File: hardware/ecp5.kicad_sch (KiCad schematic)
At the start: 6 parts, among them U3 ECP5U_12_CABGA256

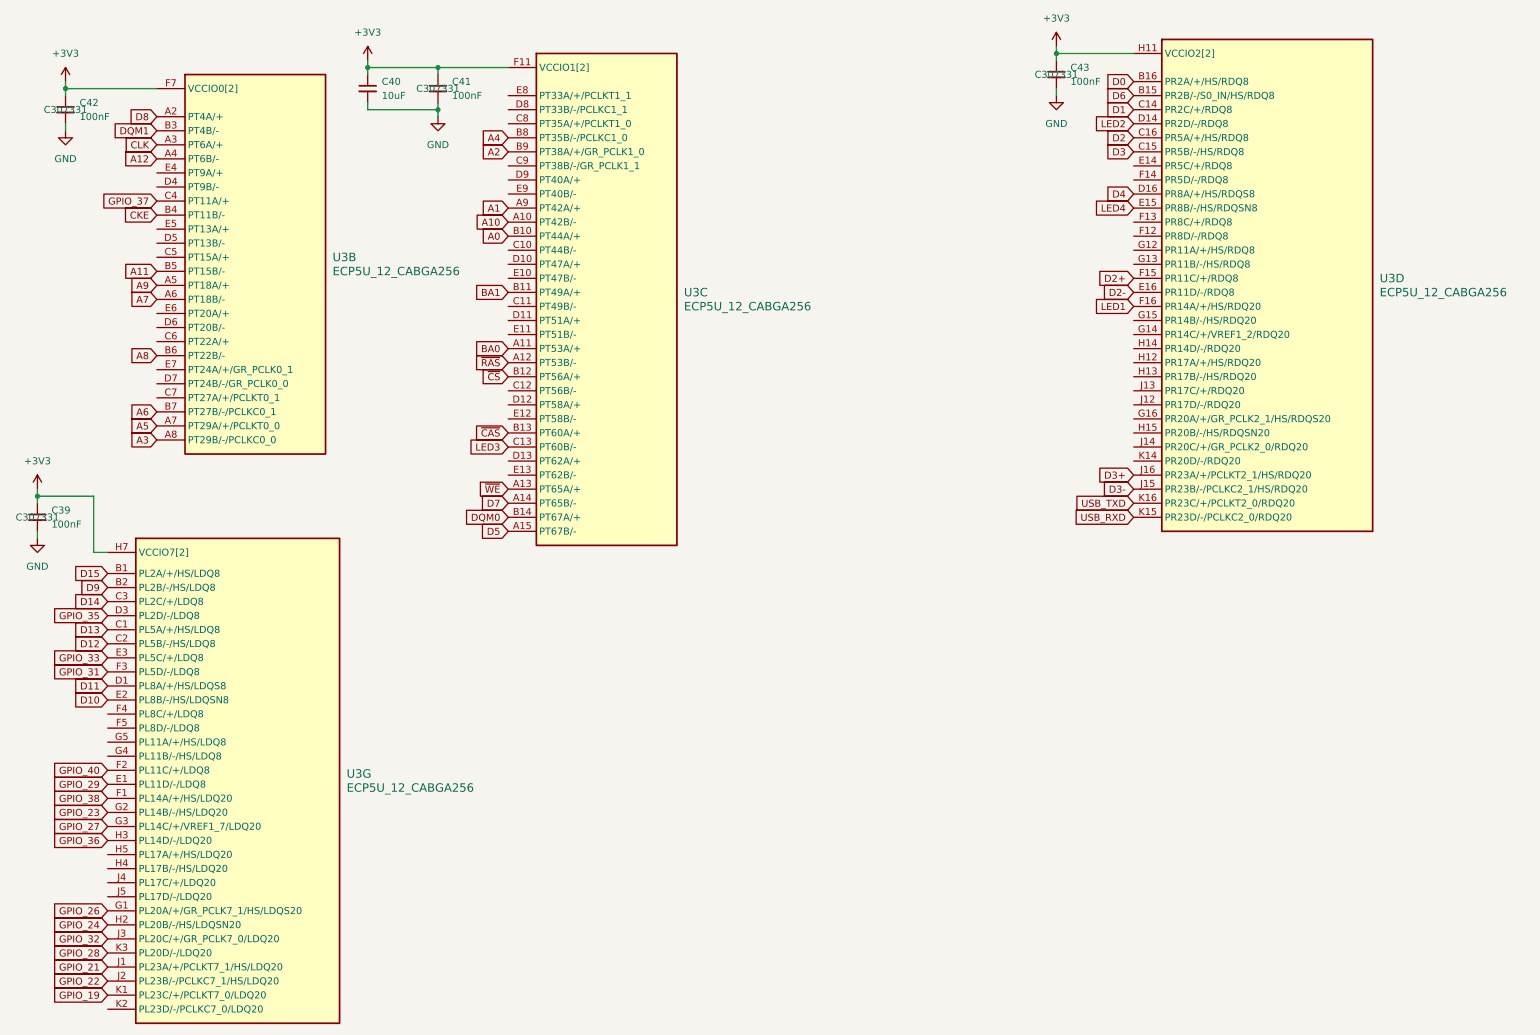
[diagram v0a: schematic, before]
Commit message: Fix level shifter EN voltage error
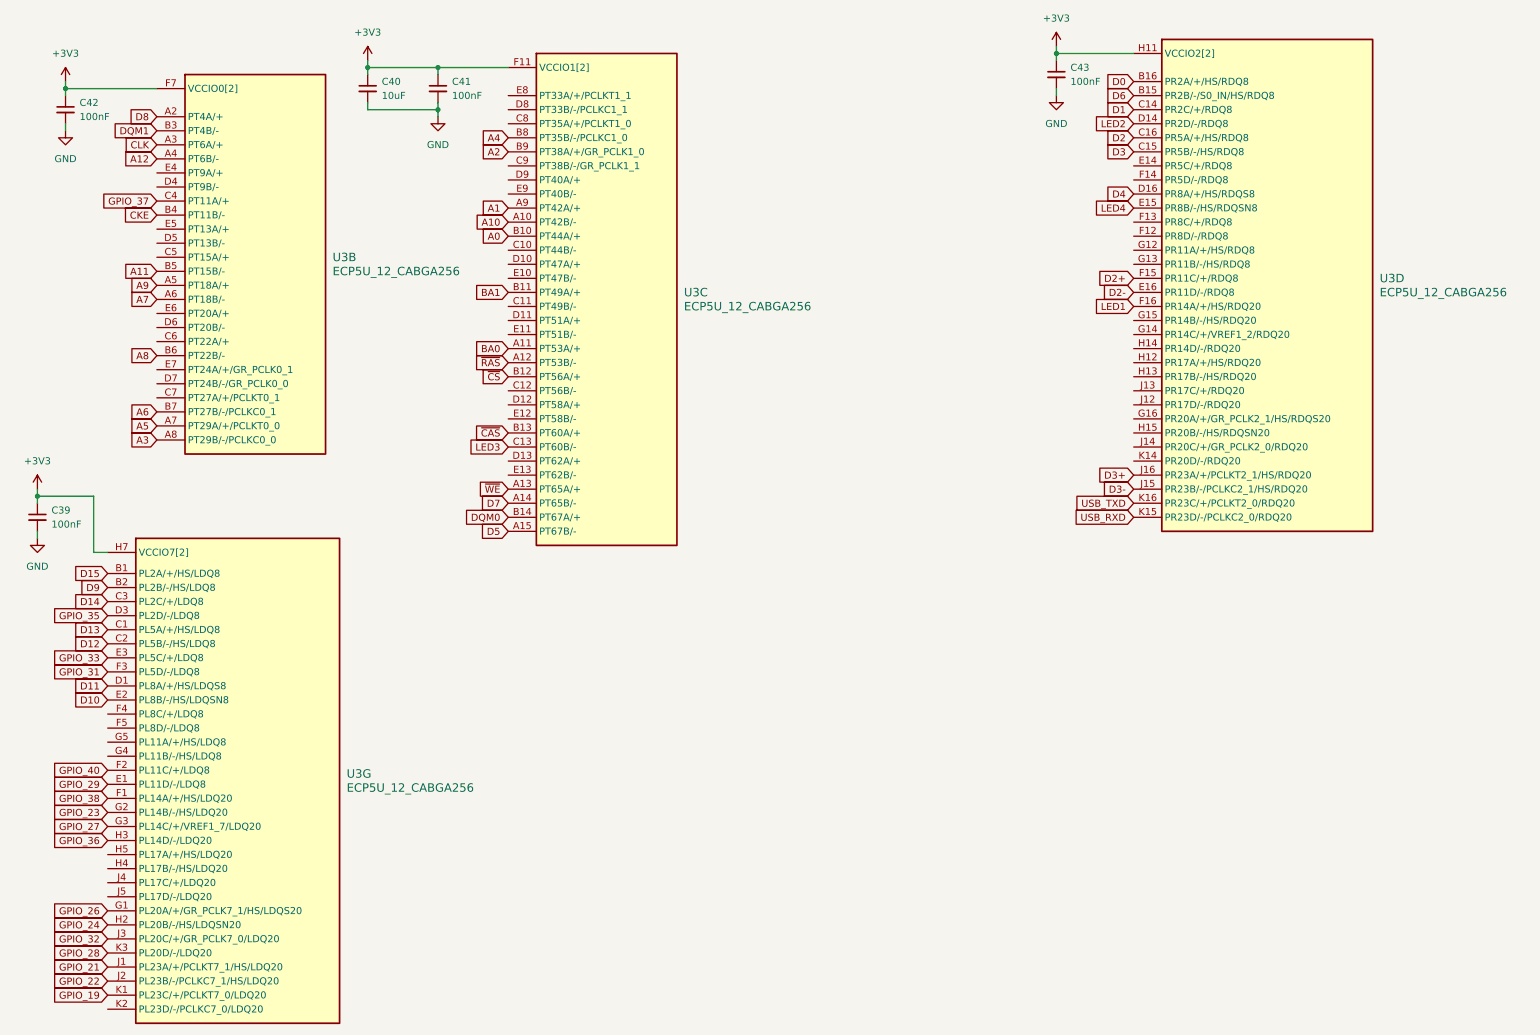
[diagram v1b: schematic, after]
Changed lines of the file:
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@@
 					(size 1.27 1.27)
 				)
+				(hide yes)
 			)
 		)
@@
 					(size 1.27 1.27)
 				)
+				(hide yes)
 			)
 		)
@@
 					(size 1.27 1.27)
 				)
+				(hide yes)
 			)
 		)
@@
 					(size 1.27 1.27)
 				)
-			)
-		)
+				(hide yes)
+			)
+		)

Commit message: Pre-prod fixes
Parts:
- added TP10, TP9: TestPoint, TestPoint:TestPoint_Pad_D2.0mm, symbol Connector:TestPoint
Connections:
- net GPIO_35: now also U3.E4 (PT9A/+); no longer U3.D3 (PL2D/-/LDQ8)
- net GPIO_37: now also U3.D4 (PT9B/-); no longer U3.C4 (PT11A/+)
- net LED2: now also U3.E15 (PR8B/-/HS/RDQSN8); no longer U3.D14 (PR2D/-/RDQ8)
- net LED3: now also U3.D14 (PR2D/-/RDQ8); no longer U3.C13 (PT60B/-)
- net LED4: now also U3.C13 (PT60B/-); no longer U3.E15 (PR8B/-/HS/RDQSN8)
- net at U3.C7 (PT27A/+/PCLKT0_1): now also TP9.1
- net at U3.C8 (PT35A/+/PCLKT1_0): now also TP10.1
- net LED5: now reaches U3.D13 (PT62A/+)
- net GPIO_19: no longer names the net of U3.K1 (PL23C/+/PCLKT7_0/LDQ20)
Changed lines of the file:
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@@
 	(wire
 		(pts
+			(xy 100.33 31.75) (xy 101.6 31.75)
+		)
+		(stroke
+			(width 0)
+			(type default)
+		)
+	)
+	(wire
+		(pts
 			(xy 21.59 31.75) (xy 21.59 33.02)
 		)
@@
 	(wire
 		(pts
+			(xy 34.29 81.28) (xy 38.1 81.28)
+		)
+		(stroke
+			(width 0)
+			(type default)
+		)
+	)
+	(wire
+		(pts
 			(xy 16.51 99.06) (xy 16.51 100.33)
 		)
@@
 		)
 	)
+	(global_label "GPIO_37"
+		(shape input)
+		(at 38.1 43.18 180)
+		(fields_autoplaced yes)
+		(effects
+			(font
+				(size 1.27 1.27)
+			)
+			(justify right)
+		)
+		(property "Intersheetrefs" "${INTERSHEET_REFS}"
+			(at 27.2529 43.18 0)
+			(effects
+				(font
+					(size 1.27 1.27)
+				)
+				(justify right)
+				(hide yes)
+			)
+		)
+	)
 	(global_label "GPIO_23"
 		(shape input)
@@
 		)
 	)
-	(global_label "GPIO_35"
-		(shape input)
-		(at 29.21 120.65 180)
-		(fields_autoplaced yes)
-		(effects
-			(font
-				(size 1.27 1.27)
-			)
-			(justify right)
-		)
-		(property "Intersheetrefs" "${INTERSHEET_REFS}"
-			(at 18.3629 120.65 0)
-			(effects
-				(font
-					(size 1.27 1.27)
-				)
-				(justify right)
-				(hide yes)
-			)
-		)
-	)
 	(global_label "D8"
 		(shape input)
@@
 		)
 	)
-	(global_label "GPIO_24"
+	(global_label "GPIO_35"
 		(shape input)
-		(at 29.21 176.53 180)
+		(at 38.1 40.64 180)
 		(fields_autoplaced yes)
 		(effects
@@
 		)
 		(property "Intersheetrefs" "${INTERSHEET_REFS}"
-			(at 18.3629 176.53 0)
+			(at 27.2529 40.64 0)
 			(effects
 				(font
@@
 		)
 	)
-	(global_label "D3"
+	(global_label "GPIO_24"
 		(shape input)
-		(at 214.63 36.83 180)
+		(at 29.21 176.53 180)
 		(fields_autoplaced yes)
 		(effects
@@
 		)
 		(property "Intersheetrefs" "${INTERSHEET_REFS}"
-			(at 209.1653 36.83 0)
+			(at 18.3629 176.53 0)
 			(effects
 				(font
@@
 		)
 	)
-	(global_label "GPIO_37"
+	(global_label "D3"
 		(shape input)
-		(at 38.1 45.72 180)
+		(at 214.63 36.83 180)
 		(fields_autoplaced yes)
 		(effects
@@
 		)
 		(property "Intersheetrefs" "${INTERSHEET_REFS}"
-			(at 27.2529 45.72 0)
+			(at 209.1653 36.83 0)
 			(effects
 				(font
@@
 		)
 	)
-	(global_label "LED2"
+	(global_label "LED3"
 		(shape input)
 		(at 214.63 31.75 180)
@@
 		)
 	)
-	(global_label "LED4"
+	(global_label "LED2"
 		(shape input)
 		(at 214.63 46.99 180)
@@
 		)
 	)
-	(global_label "GPIO_19"
+	(global_label "A0"
 		(shape input)
-		(at 29.21 189.23 180)
+		(at 101.6 52.07 180)
 		(fields_autoplaced yes)
 		(effects
@@
 		)
 		(property "Intersheetrefs" "${INTERSHEET_REFS}"
-			(at 18.3629 189.23 0)
+			(at 96.3167 52.07 0)
 			(effects
 				(font
@@
 		)
 	)
-	(global_label "A0"
+	(global_label "~{CS}"
 		(shape input)
-		(at 101.6 52.07 180)
+		(at 101.6 77.47 180)
 		(fields_autoplaced yes)
 		(effects
@@
 		)
 		(property "Intersheetrefs" "${INTERSHEET_REFS}"
-			(at 96.3167 52.07 0)
+			(at 96.1353 77.47 0)
 			(effects
 				(font
@@
 		)
 	)
-	(global_label "~{CS}"
+	(global_label "LED5"
 		(shape input)
-		(at 101.6 77.47 180)
+		(at 101.6 92.71 180)
 		(fields_autoplaced yes)
 		(effects
@@
 		)
 		(property "Intersheetrefs" "${INTERSHEET_REFS}"
-			(at 96.1353 77.47 0)
+			(at 93.9582 92.71 0)
 			(effects
 				(font
@@
 		)
 	)
-	(global_label "LED3"
+	(global_label "LED4"
 		(shape input)
 		(at 101.6 90.17 180)
@@
 	)
 	(symbol
+		(lib_id "Connector:TestPoint")
+		(at 34.29 81.28 90)
+		(unit 1)
+		(exclude_from_sim no)
+		(in_bom yes)
+		(on_board yes)
+		(dnp yes)
+		(property "Reference" "TP9"
+			(at 28.702 78.232 0)
+			(effects
+				(font
+					(size 1.27 1.27)
+				)
+				(justify right)
+			)
+		)
+		(property "Value" "TestPoint"
+			(at 26.162 78.232 0)
+			(effects
+				(font
+					(size 1.27 1.27)
+				)
+				(justify right)
+			)
+		)
+		(property "Footprint" "TestPoint:TestPoint_Pad_D2.0mm"
+			(at 34.29 76.2 0)
+			(effects
+				(font
+					(size 1.27 1.27)
+				)
+				(hide yes)
+			)
+		)
+		(property "Datasheet" "~"
+			(at 34.29 76.2 0)
+			(effects
+				(font
+					(size 1.27 1.27)
+				)
+				(hide yes)
+			)
+		)
+		(property "Description" "test point"
+			(at 34.29 81.28 0)
+			(effects
+				(font
+					(size 1.27 1.27)
+				)
+				(hide yes)
+			)
+		)
+		(pin "1"
+		)
+		(instances
+			(project "icepi-zero"
+				(path "/f88da08e-cf42-4d03-a08f-3f602fe6658d/17c9c9b3-f379-4e1f-a876-d3fcf0529a4d"
+					(reference "TP9")
+					(unit 1)
+				)
+			)
+		)
+	)
+	(symbol
 		(lib_id "josh:ECP5U_12_CABGA256")
 		(at 236.22 57.15 0)
@@
 					(unit 1)
 				)
+			)
+		)
+	)
+	(symbol
+		(lib_id "Connector:TestPoint")
+		(at 100.33 31.75 90)
+		(unit 1)
+		(exclude_from_sim no)
+		(in_bom yes)
+		(on_board yes)
+		(dnp yes)
+		(property "Reference" "TP10"
+			(at 94.742 28.702 0)
+			(effects
+				(font
+					(size 1.27 1.27)
+				)
+				(justify right)
+			)
+		)
+		(property "Value" "TestPoint"
+			(at 92.202 28.702 0)
+			(effects
+				(font
+					(size 1.27 1.27)
+				)
+				(justify right)
+			)
+		)
+		(property "Footprint" "TestPoint:TestPoint_Pad_D2.0mm"
+			(at 100.33 26.67 0)
+			(effects
+				(font
+					(size 1.27 1.27)
+				)
+				(hide yes)
+			)
+		)
+		(property "Datasheet" "~"
+			(at 100.33 26.67 0)
+			(effects
+				(font
+					(size 1.27 1.27)
+				)
+				(hide yes)
+			)
+		)
+		(property "Description" "test point"
+			(at 100.33 31.75 0)
+			(effects
+				(font
+					(size 1.27 1.27)
+				)
+				(hide yes)
+			)
+		)
+		(pin "1"
+		)
+		(instances
+			(project "icepi-zero"
+				(path "/f88da08e-cf42-4d03-a08f-3f602fe6658d/17c9c9b3-f379-4e1f-a876-d3fcf0529a4d"
+					(reference "TP10")
+					(unit 1)
+				)

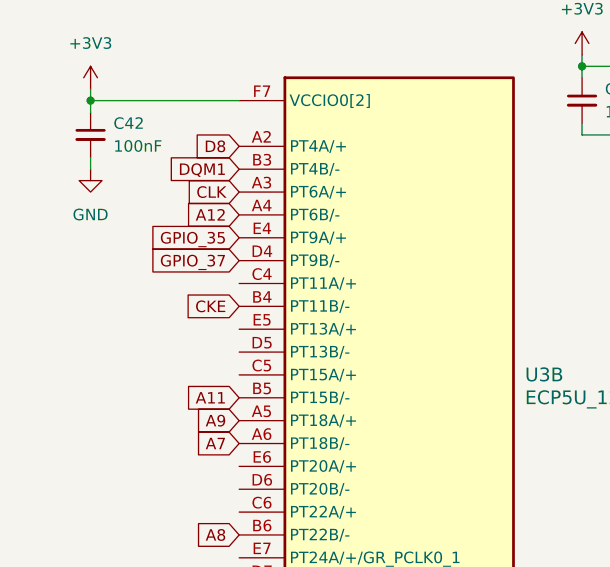
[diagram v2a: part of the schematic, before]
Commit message: Add a button
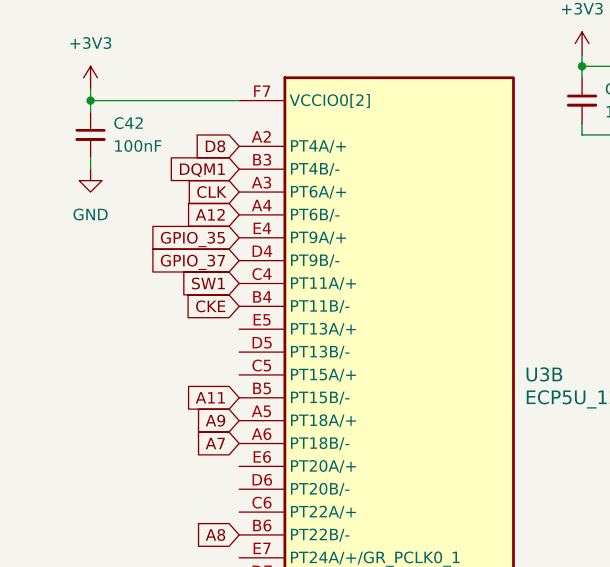
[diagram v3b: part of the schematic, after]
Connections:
- net SW1: now reaches U3.C4 (PT11A/+)
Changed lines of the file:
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@@
+		)
+	)
+	(global_label "SW1"
+		(shape input)
+		(at 38.1 45.72 180)
+		(fields_autoplaced yes)
+		(effects
+			(font
+				(size 1.27 1.27)
+			)
+			(justify right)
+		)
+		(property "Intersheetrefs" "${INTERSHEET_REFS}"
+			(at 31.2444 45.72 0)
+			(effects
+				(font
+					(size 1.27 1.27)
+				)
+				(justify right)
+				(hide yes)
+			)
 		)
 	)

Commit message: Final revision
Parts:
- C39, C41, C42, C43: JLCPCB Part # C307331 -> (none); LCSC Part # (none) -> C307331
- U3: JLCPCB Part # C1521614 -> (none); LCSC Part # (none) -> C1521614
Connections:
- net DBG1: now reaches TP9.1, U3.C7 (PT27A/+/PCLKT0_1)
- net DBG2: now reaches TP10.1, U3.C8 (PT35A/+/PCLKT1_0)
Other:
- moved on the sheet: C39, C40, C41, TP10, U3G

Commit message: Last checks
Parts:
- C49: renamed from C40; LCSC Part # (none) -> C19702
- renumbered C43 to C48, C41 to C50, C42 to C51, C39 to C52, TP10 to TP13, TP9 to TP14, U3 to U1
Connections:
- no-connect marks 0 -> 51
